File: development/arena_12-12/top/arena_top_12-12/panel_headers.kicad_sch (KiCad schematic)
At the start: 24 parts, among them P1 CONN15, P10 CONN15, P11 CONN15, P12 CONN15, P2 CONN15, P3 CONN15, P4 CONN15, P5 CONN15, P6 CONN15, P7 CONN15, P8 CONN15, P9 CONN15

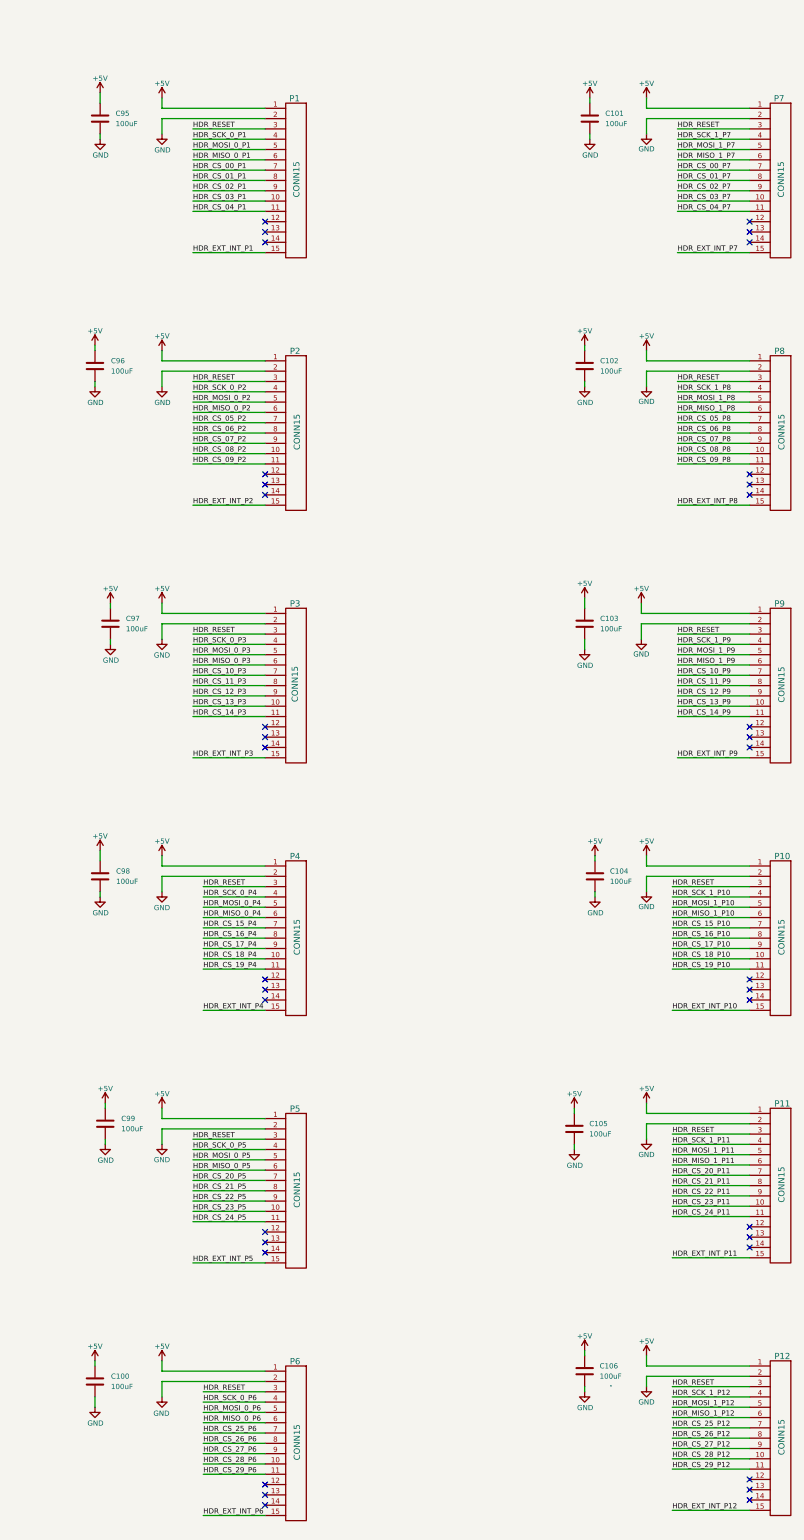
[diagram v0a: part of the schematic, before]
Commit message: Finished hand route of 12-12 teensy arena. Finished route of 12-12 top.
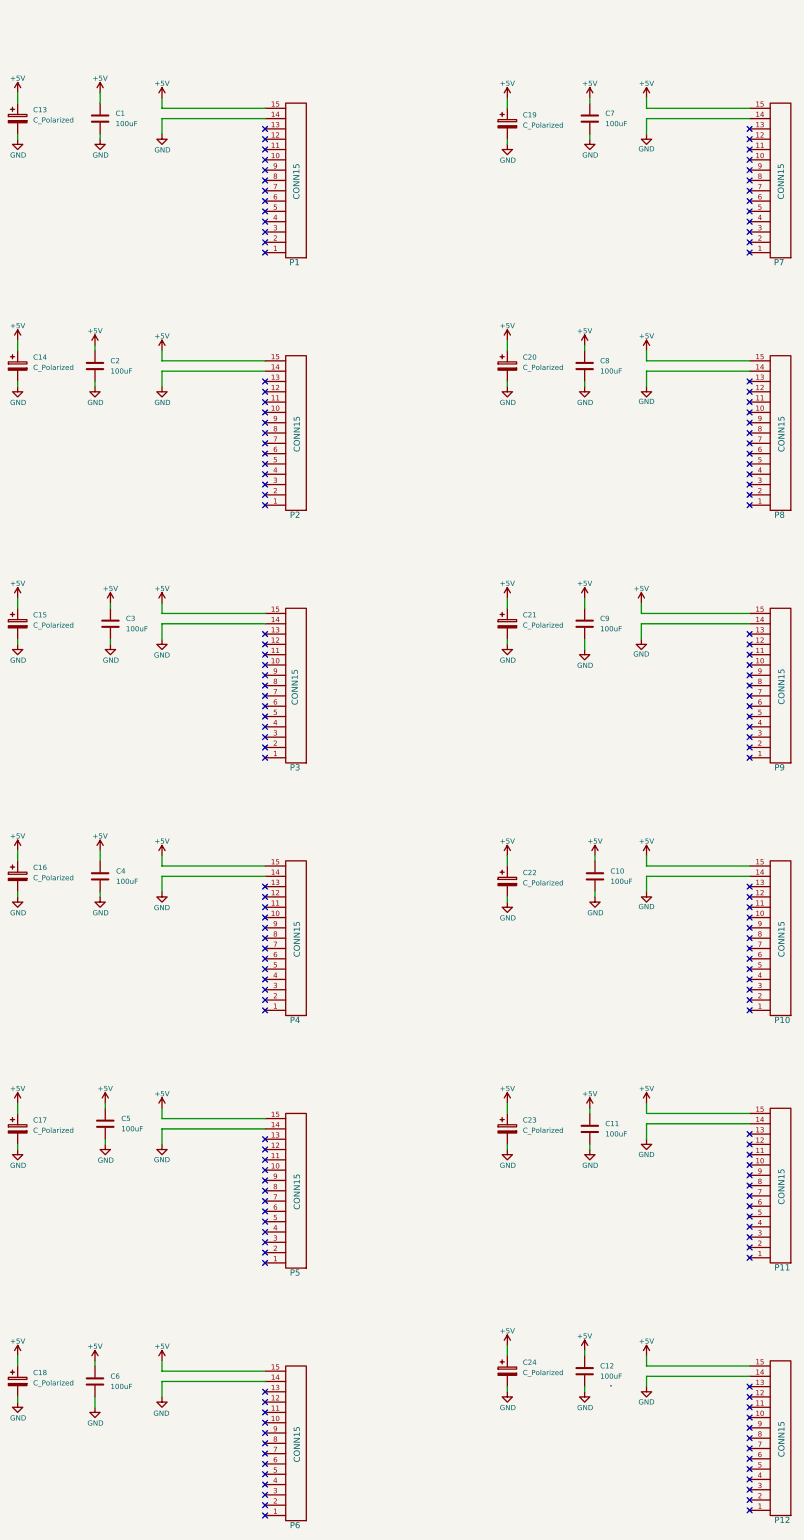
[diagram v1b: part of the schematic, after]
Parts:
- added C13, C14, C15, C16, C17, C18, C19, C20, C21, C22, C23, C24: C_Polarized, Capacitor_THT:CP_Radial_D8.0mm_P2.50mm, symbol Device:C_Polarized
- renumbered C95 to C1, C104 to C10, C105 to C11, C106 to C12, C96 to C2, C97 to C3, C98 to C4, C99 to C5, C100 to C6, C101 to C7, C102 to C8, C103 to C9
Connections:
- net HDR_EXT_INT_P1 is gone; now on net +5V: P1.15
- net HDR_EXT_INT_P10 is gone; now on net +5V: P10.15
- net HDR_EXT_INT_P11 is gone; now on net +5V: P11.15
- net HDR_EXT_INT_P12 is gone; now on net +5V: P12.15
- net HDR_EXT_INT_P2 is gone; now on net +5V: P2.15
- net HDR_EXT_INT_P3 is gone; now on net +5V: P3.15
- net HDR_EXT_INT_P4 is gone; now on net +5V: P4.15
- net HDR_EXT_INT_P5 is gone; now on net +5V: P5.15
- net HDR_EXT_INT_P6 is gone; now on net +5V: P6.15
- net HDR_EXT_INT_P7 is gone; now on net +5V: P7.15
- net HDR_EXT_INT_P8 is gone; now on net +5V: P8.15
- net HDR_EXT_INT_P9 is gone; now on net +5V: P9.15
- net +5V: now also C13.1, C14.1, C15.1, C16.1, C17.1, C18.1, C19.1, C20.1, C21.1, C22.1, C23.1, C24.1; no longer P1.1, P10.1, P11.1, P12.1, P2.1, P3.1, P4.1, P5.1, P6.1, P7.1, P8.1, P9.1
- net GND: now also P1.14, P10.14, P11.14, P12.14, P2.14, P3.14, P4.14, P5.14, P6.14, P7.14, P8.14, P9.14, C13.2, C14.2, C15.2, C16.2, C17.2, C18.2, C19.2, C20.2, C21.2, C22.2, C23.2, C24.2; no longer P1.2, P10.2, P11.2, P12.2, P2.2, P3.2, P4.2, P5.2, P6.2, P7.2, P8.2, P9.2
- net HDR_CS_00_P1: no longer names the net of P1.7
- net HDR_CS_00_P7: no longer names the net of P7.7
- net HDR_CS_01_P1: no longer names the net of P1.8
- net HDR_CS_01_P7: no longer names the net of P7.8
- net HDR_CS_02_P1: no longer names the net of P1.9
- net HDR_CS_02_P7: no longer names the net of P7.9
- net HDR_CS_03_P1: no longer names the net of P1.10
- net HDR_CS_03_P7: no longer names the net of P7.10
- net HDR_CS_04_P1: no longer names the net of P1.11
- net HDR_CS_04_P7: no longer names the net of P7.11
- net HDR_CS_05_P2: no longer names the net of P2.7
- net HDR_CS_05_P8: no longer names the net of P8.7
- net HDR_CS_06_P2: no longer names the net of P2.8
- net HDR_CS_06_P8: no longer names the net of P8.8
- net HDR_CS_07_P2: no longer names the net of P2.9
- net HDR_CS_07_P8: no longer names the net of P8.9
- net HDR_CS_08_P2: no longer names the net of P2.10
- net HDR_CS_08_P8: no longer names the net of P8.10
- net HDR_CS_09_P2: no longer names the net of P2.11
- net HDR_CS_09_P8: no longer names the net of P8.11
- net HDR_CS_10_P3: no longer names the net of P3.7
- net HDR_CS_10_P9: no longer names the net of P9.7
- net HDR_CS_11_P3: no longer names the net of P3.8
- net HDR_CS_11_P9: no longer names the net of P9.8
- net HDR_CS_12_P3: no longer names the net of P3.9
- net HDR_CS_12_P9: no longer names the net of P9.9
- net HDR_CS_13_P3: no longer names the net of P3.10
- net HDR_CS_13_P9: no longer names the net of P9.10
- net HDR_CS_14_P3: no longer names the net of P3.11
- net HDR_CS_14_P9: no longer names the net of P9.11
- net HDR_CS_15_P10: no longer names the net of P10.7
- net HDR_CS_15_P4: no longer names the net of P4.7
- net HDR_CS_16_P10: no longer names the net of P10.8
- net HDR_CS_16_P4: no longer names the net of P4.8
- net HDR_CS_17_P10: no longer names the net of P10.9
- net HDR_CS_17_P4: no longer names the net of P4.9
- net HDR_CS_18_P10: no longer names the net of P10.10
- net HDR_CS_18_P4: no longer names the net of P4.10
- net HDR_CS_19_P10: no longer names the net of P10.11
- net HDR_CS_19_P4: no longer names the net of P4.11
- net HDR_CS_20_P11: no longer names the net of P11.7
- net HDR_CS_20_P5: no longer names the net of P5.7
- net HDR_CS_21_P11: no longer names the net of P11.8
- net HDR_CS_21_P5: no longer names the net of P5.8
- net HDR_CS_22_P11: no longer names the net of P11.9
- net HDR_CS_22_P5: no longer names the net of P5.9
- net HDR_CS_23_P11: no longer names the net of P11.10
- net HDR_CS_23_P5: no longer names the net of P5.10
- net HDR_CS_24_P11: no longer names the net of P11.11
- net HDR_CS_24_P5: no longer names the net of P5.11
- net HDR_CS_25_P12: no longer names the net of P12.7
- net HDR_CS_25_P6: no longer names the net of P6.7
- net HDR_CS_26_P12: no longer names the net of P12.8
- net HDR_CS_26_P6: no longer names the net of P6.8
- net HDR_CS_27_P12: no longer names the net of P12.9
- net HDR_CS_27_P6: no longer names the net of P6.9
- net HDR_CS_28_P12: no longer names the net of P12.10
- net HDR_CS_28_P6: no longer names the net of P6.10
- net HDR_CS_29_P12: no longer names the net of P12.11
- net HDR_CS_29_P6: no longer names the net of P6.11
- net HDR_MISO_0_P1: no longer names the net of P1.6
- net HDR_MISO_0_P2: no longer names the net of P2.6
- net HDR_MISO_0_P3: no longer names the net of P3.6
- net HDR_MISO_0_P4: no longer names the net of P4.6
- net HDR_MISO_0_P5: no longer names the net of P5.6
- net HDR_MISO_0_P6: no longer names the net of P6.6
- net HDR_MISO_1_P10: no longer names the net of P10.6
- net HDR_MISO_1_P11: no longer names the net of P11.6
- net HDR_MISO_1_P12: no longer names the net of P12.6
- net HDR_MISO_1_P7: no longer names the net of P7.6
- net HDR_MISO_1_P8: no longer names the net of P8.6
- net HDR_MISO_1_P9: no longer names the net of P9.6
- net HDR_MOSI_0_P1: no longer names the net of P1.5
- net HDR_MOSI_0_P2: no longer names the net of P2.5
- net HDR_MOSI_0_P3: no longer names the net of P3.5
- net HDR_MOSI_0_P4: no longer names the net of P4.5
- net HDR_MOSI_0_P5: no longer names the net of P5.5
- net HDR_MOSI_0_P6: no longer names the net of P6.5
- net HDR_MOSI_1_P10: no longer names the net of P10.5
- net HDR_MOSI_1_P11: no longer names the net of P11.5
- net HDR_MOSI_1_P12: no longer names the net of P12.5
- net HDR_MOSI_1_P7: no longer names the net of P7.5
- net HDR_MOSI_1_P8: no longer names the net of P8.5
- net HDR_MOSI_1_P9: no longer names the net of P9.5
- removed net HDR_RESET: P1.3, P10.3, P11.3, P12.3, P2.3, P3.3, P4.3, P5.3, P6.3, P7.3, P8.3, P9.3
- net HDR_SCK_0_P1: no longer names the net of P1.4
- net HDR_SCK_0_P2: no longer names the net of P2.4
- net HDR_SCK_0_P3: no longer names the net of P3.4
- net HDR_SCK_0_P4: no longer names the net of P4.4
- net HDR_SCK_0_P5: no longer names the net of P5.4
- net HDR_SCK_0_P6: no longer names the net of P6.4
- net HDR_SCK_1_P10: no longer names the net of P10.4
- net HDR_SCK_1_P11: no longer names the net of P11.4
- net HDR_SCK_1_P12: no longer names the net of P12.4
- net HDR_SCK_1_P7: no longer names the net of P7.4
- net HDR_SCK_1_P8: no longer names the net of P8.4
- net HDR_SCK_1_P9: no longer names the net of P9.4
- no-connect marks 36 -> 156
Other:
- moved on the sheet: C11
